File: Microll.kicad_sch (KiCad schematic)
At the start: 12 parts, among them J1 USB_C_Receptacle, U2 STM32G0B1CBU6, U3 ESP32-C3-WROOM-02-N4, U4 LSM6DSL

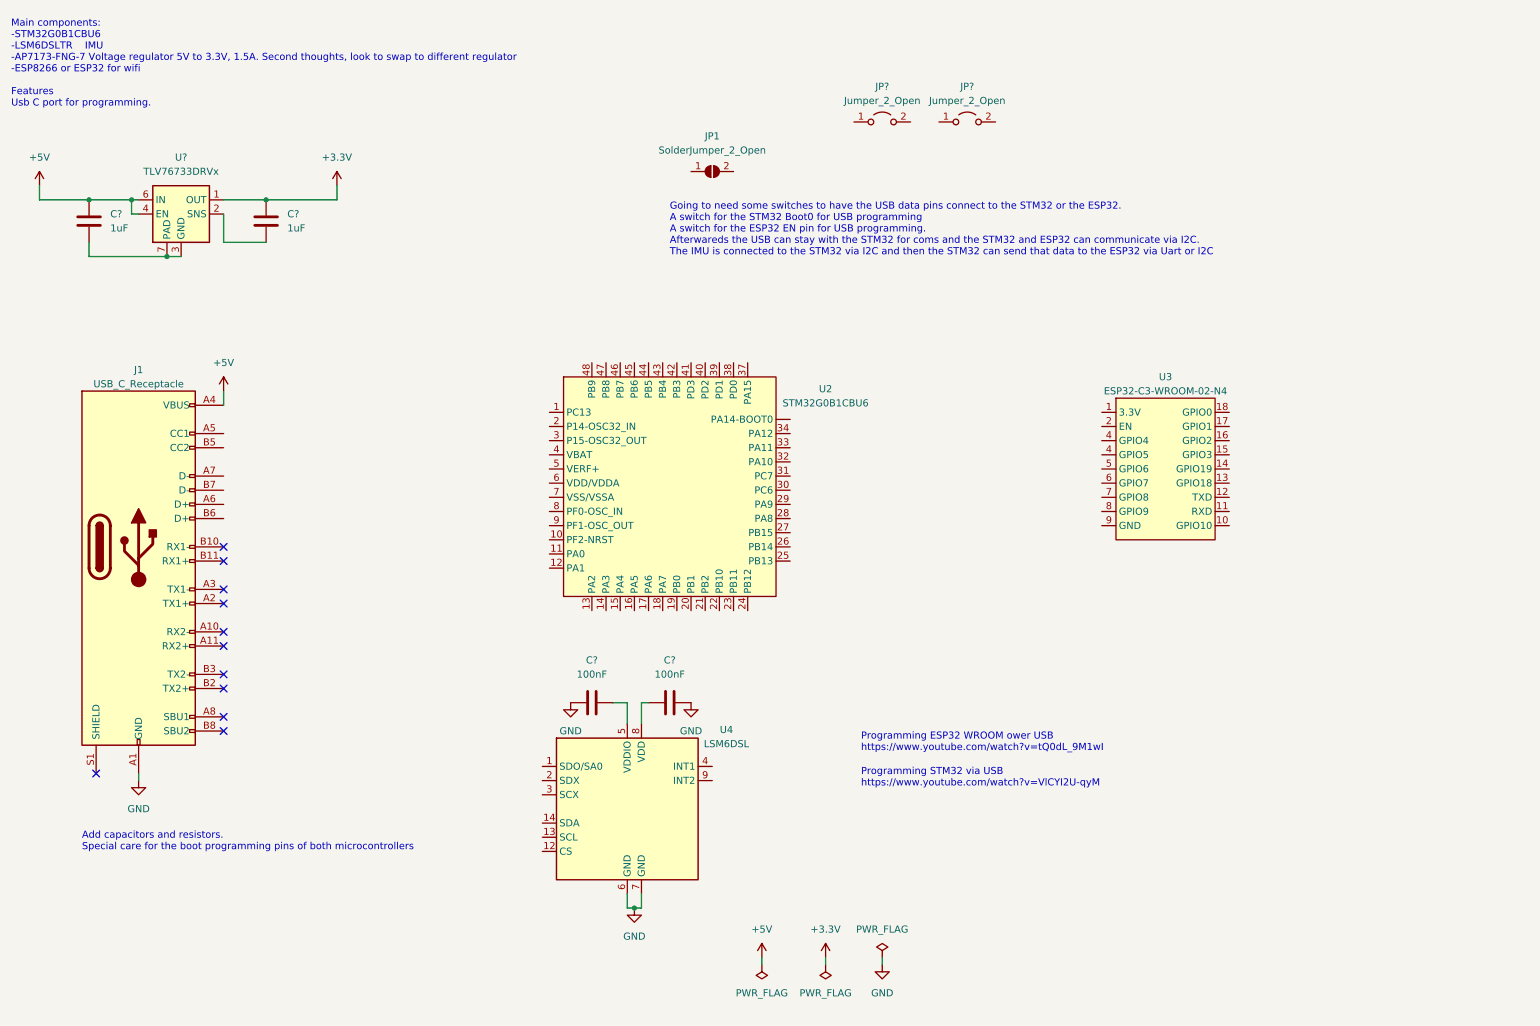
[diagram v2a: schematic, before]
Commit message: Added 3D models to all PCB components. Added switch for USB programming between microcontrollers
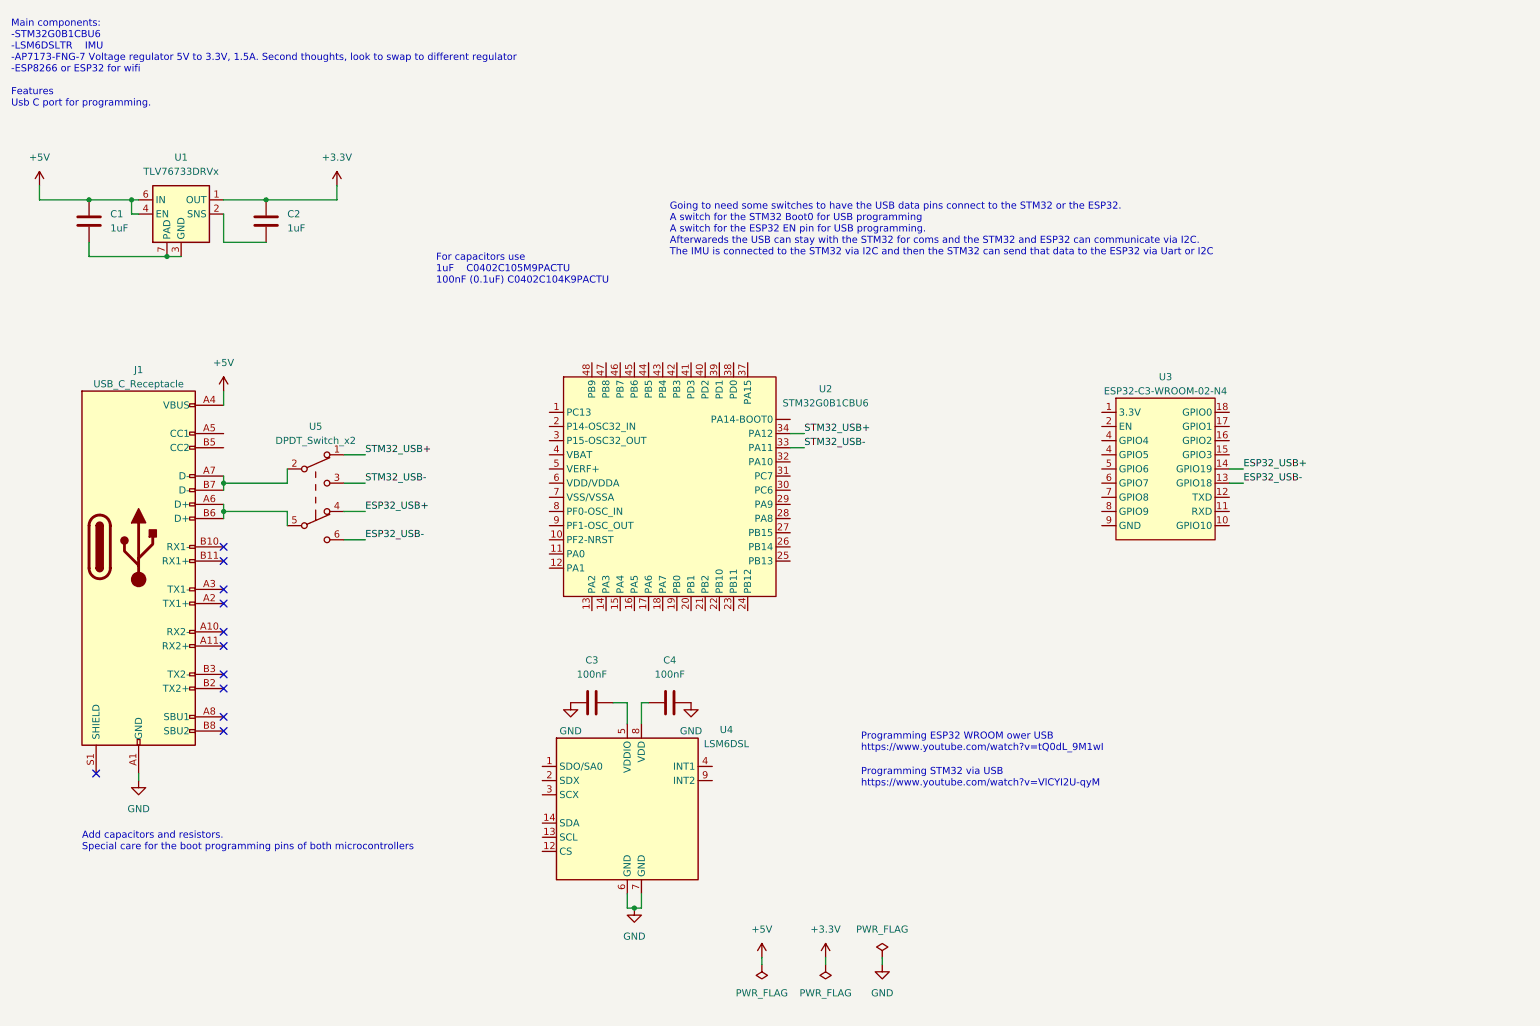
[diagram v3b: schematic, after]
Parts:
- removed JP1: SolderJumper_2_Open, SolderJumper-2_P1.3mm_Open_RoundedPad1.0x1.5mm, symbol Jumper:SolderJumper_2_Open
- removed JP? (x2): Jumper_2_Open, symbol Jumper:Jumper_2_Open
- added U5: DPDT_Switch_x2, DPDT_Switch_x2:DPDT_Switch_x2, symbol DPDT_Switch_x2:DPDT_Switch_x2
- C1, C2, C3, C4: renamed from C?; footprint (none) -> Capacitor_SMD:C_0402_1005Metric
- gave numbers to parts that had none: 1
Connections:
- net ESP32_USB-: now reaches U3.13 (GPIO18)
- net ESP32_USB-: now also U5.6
- net ESP32_USB+: now reaches U3.14 (GPIO19)
- net ESP32_USB+: now also U5.4
- net STM32_USB-: now reaches U2.33 (PA11)
- net STM32_USB-: now also U5.3
- net STM32_USB+: now reaches U2.34 (PA12)
- net STM32_USB+: now also U5.1
- net at J1.A6 (D+): now also J1.B6 (D+), U5.5
- net at J1.A7 (D-): now also J1.B7 (D-), U5.2
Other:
- note added: "For capacitors use 1uF C0402C105M9PACTU 100nF (0.1uF) C0402C104K9PACTU"

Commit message: Added todo list
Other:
- note added: "TODOs: Add decoupling capacitors to STM32 Add IO slots to the PCB itself Add I2C communication between STM32 AND ESP32 Add connection between STM32 and IMU"
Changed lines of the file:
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@@
+    (effects (font (size 1.27 1.27)) (justify left bottom))
+  )
+  (text "TODOs:\nAdd decoupling capacitors to STM32\nAdd IO slots to the PCB itself\nAdd I2C communication between STM32 AND ESP32\nAdd connection between STM32 and IMU"
+    (at 147.32 31.75 0)
     (effects (font (size 1.27 1.27)) (justify left bottom))
   )

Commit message: Corrected mistake in usb wiring to switch
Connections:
- net ESP32_USB+: now also U5.3; no longer U5.4
- net STM32_USB-: now also U5.4; no longer U5.3
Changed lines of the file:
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@@
+    (stroke (width 0) (type default) (color 0 0 0 0))
+  )
+  (wire (pts (xy 74.93 99.06) (xy 78.74 99.06))
     (stroke (width 0) (type default) (color 0 0 0 0))
   )
@@
     (stroke (width 0) (type default) (color 0 0 0 0))
   )
-  (wire (pts (xy 74.93 99.06) (xy 78.74 99.06))
-    (stroke (width 0) (type default) (color 0 0 0 0))
-  )
   (wire (pts (xy 125.73 172.72) (xy 125.73 175.26))
     (stroke (width 0) (type default) (color 0 0 0 0))
@@
     (stroke (width 0) (type default) (color 0 0 0 0))
   )
+  (wire (pts (xy 74.93 104.14) (xy 78.74 104.14))
+    (stroke (width 0) (type default) (color 0 0 0 0))
+  )
   (wire (pts (xy 233.68 96.52) (xy 236.22 96.52))
     (stroke (width 0) (type default) (color 0 0 0 0))
@@
   )
   (wire (pts (xy 29.21 58.42) (xy 29.21 55.88))
-    (stroke (width 0) (type default) (color 0 0 0 0))
-  )
-  (wire (pts (xy 74.93 104.14) (xy 78.74 104.14))
     (stroke (width 0) (type default) (color 0 0 0 0))
   )
@@
     (effects (font (size 1.27 1.27)) (justify left bottom))
   )
-  (label "ESP32_USB+" (at 78.74 104.14 0)
+  (label "ESP32_USB+" (at 78.74 99.06 0)
     (effects (font (size 1.27 1.27)) (justify left bottom))
   )
@@
     (effects (font (size 1.27 1.27)) (justify left bottom))
   )
-  (label "STM32_USB-" (at 78.74 99.06 0)
+  (label "STM32_USB-" (at 78.74 104.14 0)
     (effects (font (size 1.27 1.27)) (justify left bottom))
   )

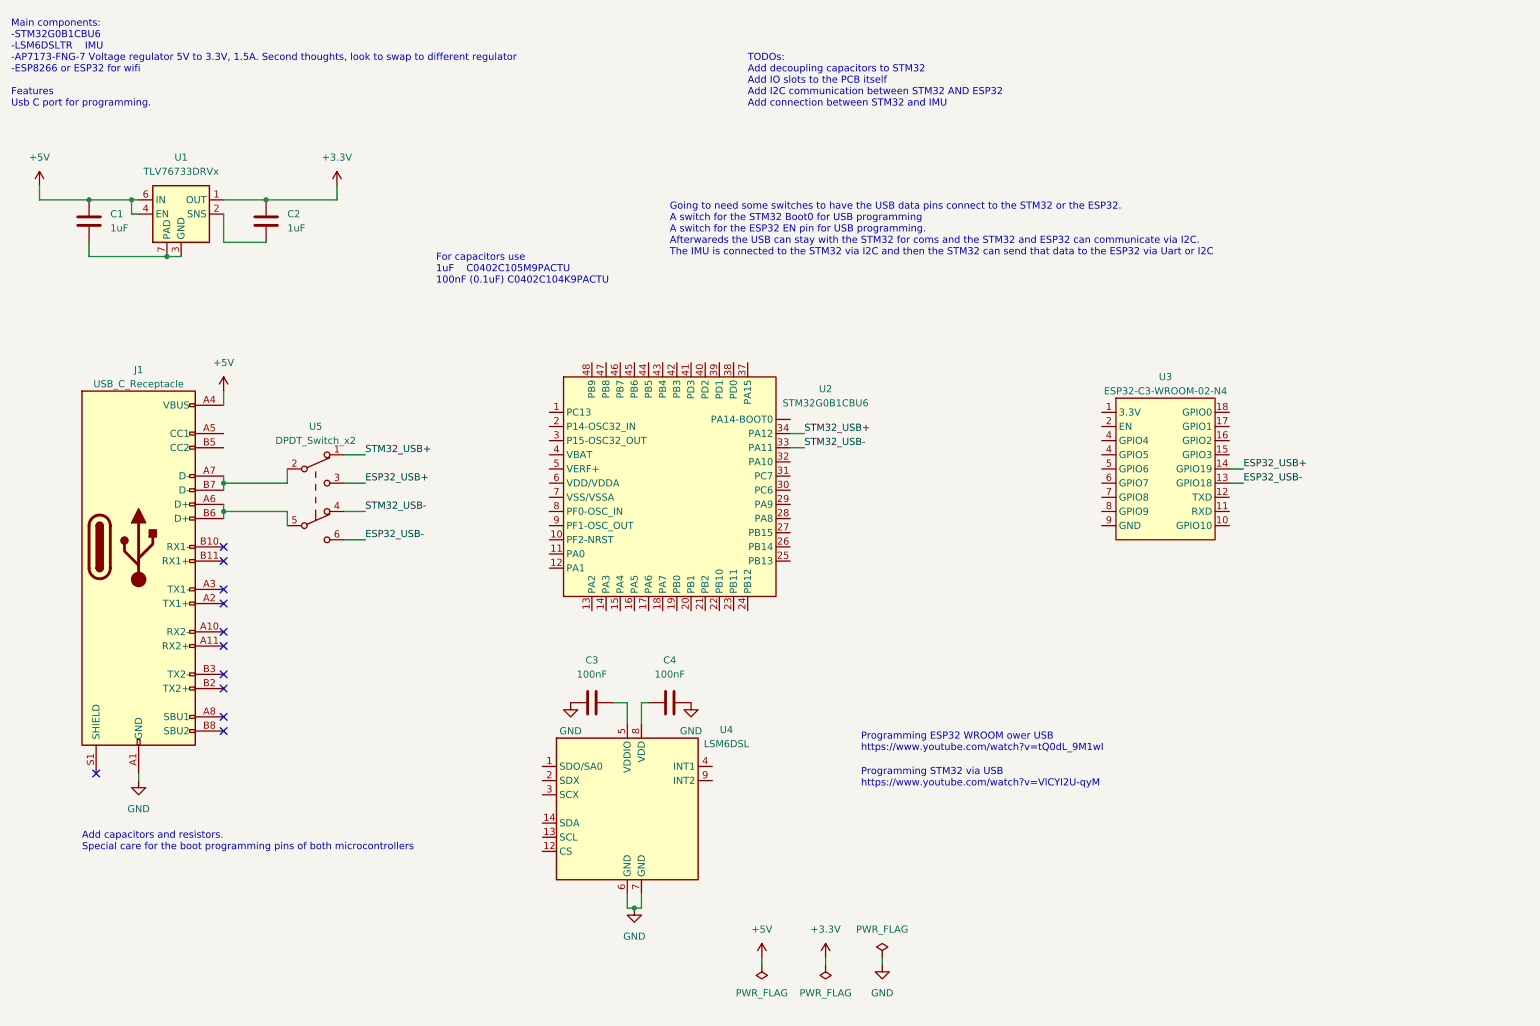
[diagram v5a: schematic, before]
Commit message: Added ESD protection, decoupling capacitors and new footprints
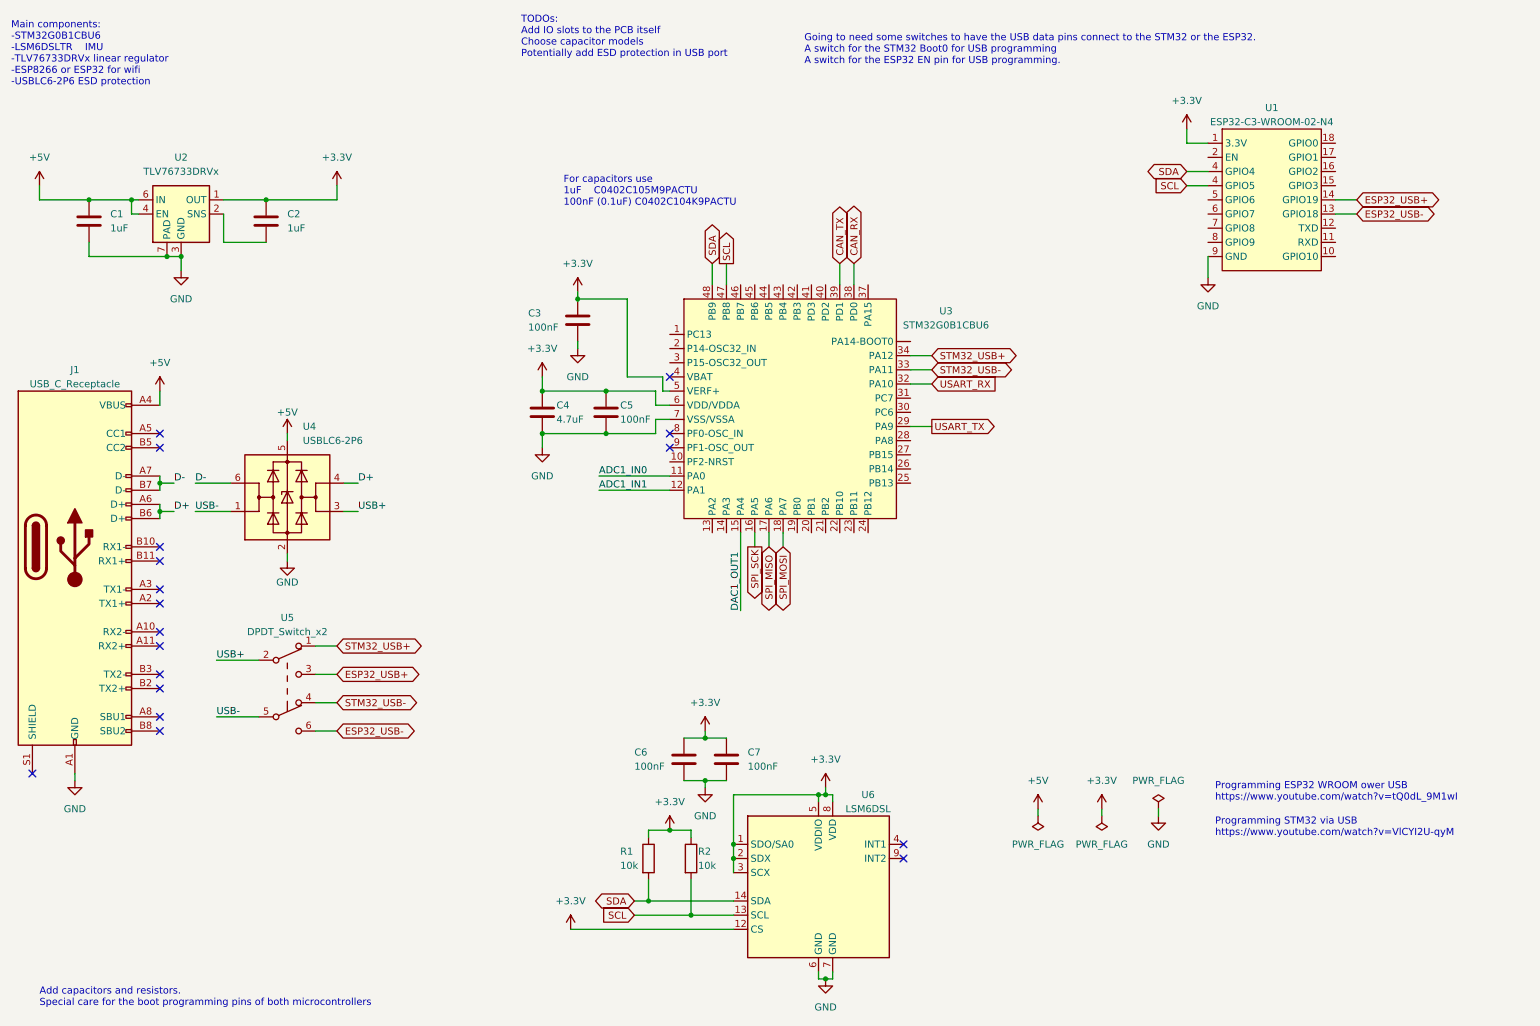
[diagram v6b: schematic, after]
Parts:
- added C4: 4.7uF, Capacitor_SMD:C_0805_2012Metric, symbol Device:C
- added C5, C6: 100nF, Capacitor_SMD:C_0402_1005Metric, symbol Device:C
- added R1, R2: 10k, Resistor_SMD:R_0402_1005Metric, symbol Device:R
- added U4: USBLC6-2P6, Package_TO_SOT_SMD:SOT-666, symbol Power_Protection:USBLC6-2P6
- renumbered C4 to C7, U3 to U1, U1 to U2, U2 to U3, U4 to U6
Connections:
- net +3.3V: now also C3.1, C7.1, U1.1 (3.3V), U3.5 (VERF+), U3.6 (VDD/VDDA), U6.1 (SDO/SA0), U6.12 (CS), U6.2 (SDX), U6.3 (SCX), U6.5 (VDDIO), U6.8 (VDD), C4.1, C5.1, C6.1, R1.1, R2.1
- net +5V: now also U4.5 (VBUS)
- net GND: now also C1.2, U1.9 (GND), U2.3 (GND), U2.5 (GND), U2.7 (PAD), U3.7 (VSS/VSSA), C4.2, C5.2, C6.2, U4.2 (GND)
- net SDA: now reaches U1.4 (GPIO5)
- net SDA: now also U3.48 (PB9), U6.14 (SDA), R1.2
- net ADC1_IN0: now reaches U3.11 (PA0)
- net ADC1_IN1: now reaches U3.12 (PA1)
- net DAC1_OUT1: now reaches U3.15 (PA4)
- net SPI_SCK: now reaches U3.16 (PA5)
- net SPI_MISO: now reaches U3.17 (PA6)
- net SPI_MOSI: now reaches U3.18 (PA7)
- net USART_TX: now reaches U3.29 (PA9)
- net USART_RX: now reaches U3.32 (PA10)
- net CAN_RX: now reaches U3.38 (PD0)
- net CAN_TX: now reaches U3.39 (PD1)
- net SCL: now reaches U3.47 (PB8)
- net SCL: now also U1.4 (GPIO5), U6.13 (SCL), R2.2
- net D+: now reaches J1.A6 (D+), J1.B6 (D+)
- net D+: now also U4.4 (I/O2); no longer U5.5
- net D-: now reaches J1.A7 (D-), J1.B7 (D-)
- net D-: now also U4.6 (I/O1); no longer U5.2
- new net USB+: U4.3 (I/O2), U5.2
- new net USB-: U4.1 (I/O1), U5.5
- no-connect marks 11 -> 18
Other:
- note added: "Going to need some switches to have the USB data pins connect to the STM32 or the ESP32. A switch for the STM32 Boot0 for USB programming A switch for the ESP32 EN pin for USB programming."
- note added: "Main components: -STM32G0B1CBU6 -LSM6DSLTR IMU -TLV76733DRVx linear regulator -ESP8266 or ESP32 for wifi -USBLC6-2P6 ESD protection"
- note added: "TODOs: Add IO slots to the PCB itself Choose capacitor models Potentially add ESD protection in USB port"
- note removed: "Going to need some switches to have the USB data pins connect to the STM32 or the ESP32. A switch for the STM32 Boot0 for USB programming A switch for the ESP32 EN pin for USB programming. Afterwareds the USB can stay with the STM32 for coms and the STM32 and ESP32 can communicate via I2C. The IMU is connected to the STM32 via I2C and then the STM32 can send that data to the ESP32 via Uart or I2C"
- note removed: "Main components: -STM32G0B1CBU6 -LSM6DSLTR IMU -AP7173-FNG-7 Voltage regulator 5V to 3.3V, 1.5A. Second thoughts, look to swap to different regulator -ESP8266 or ESP32 for wifi Features Usb C port for programming."
- note removed: "TODOs: Add decoupling capacitors to STM32 Add IO slots to the PCB itself Add I2C communication between STM32 AND ESP32 Add connection between STM32 and IMU"
- moved on the sheet: C7, J1, U1, U3, U5, U6
